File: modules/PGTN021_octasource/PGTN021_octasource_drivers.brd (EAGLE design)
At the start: 69.8 x 100.3 mm, 136 parts, among them IC1 TL084P, IC2 TL084P, IC3 TL084P, IC4 TL084P

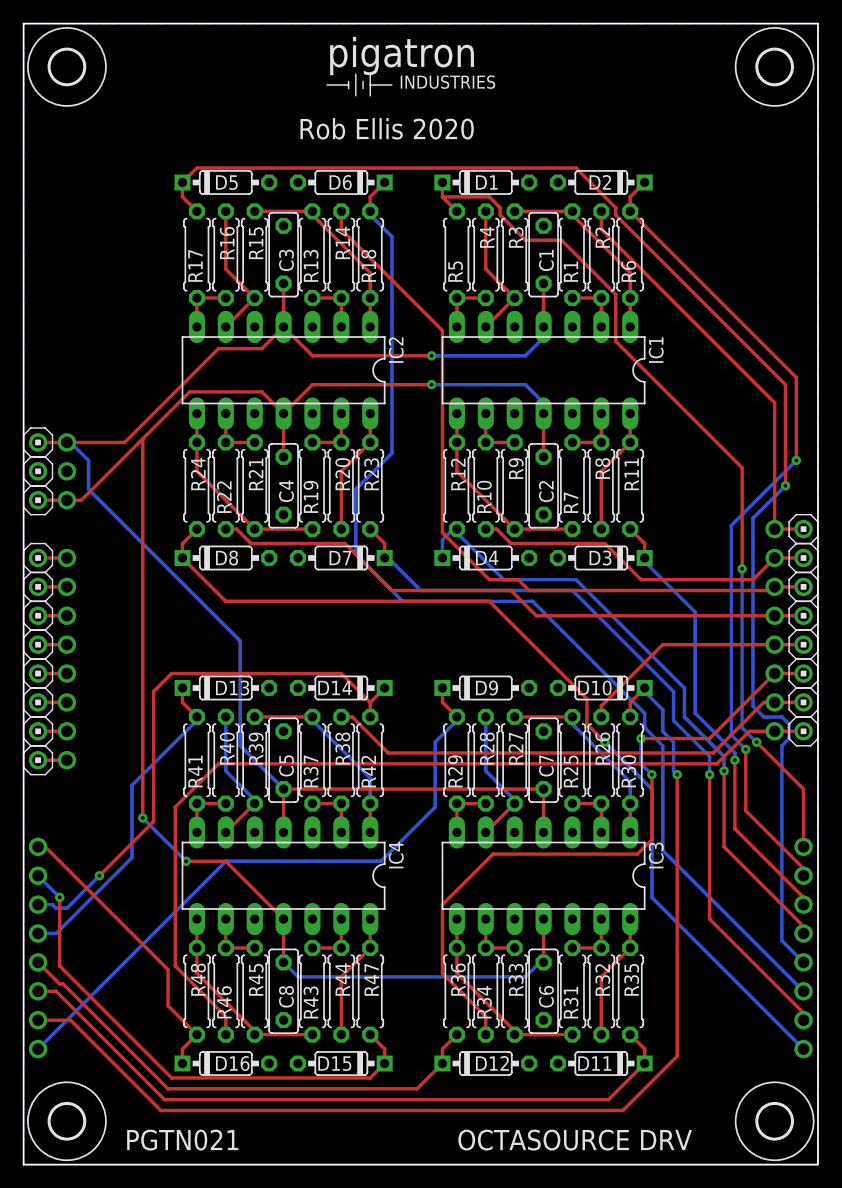
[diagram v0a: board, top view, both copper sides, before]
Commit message: Modified boards to fit together better
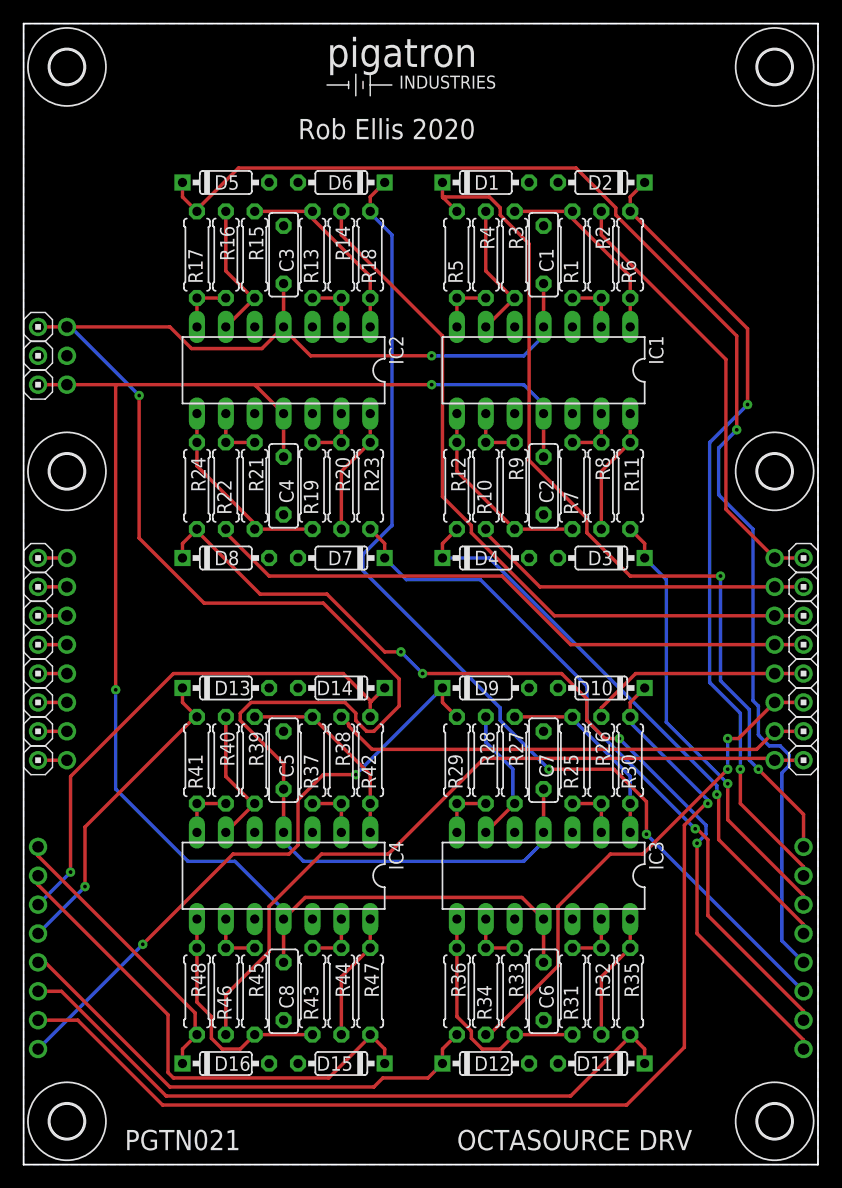
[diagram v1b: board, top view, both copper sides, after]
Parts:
- added U$4, U$5: (no value), mechanical:STANDOFF/3.0
- moved TRIG_IN 15.2 mm to (3.81, 53.3)
- moved TRIG_IN1 15.2 mm to (1.27, 53.3)
- moved GND 10.2 mm to (3.81, 71.1)
- moved GND1 10.2 mm to (1.27, 71.1)
- moved +12V 10.2 mm to (3.81, 73.7)
- moved +12V1 10.2 mm to (1.27, 73.7)
- moved -12V 10.2 mm to (3.81, 68.6)
- moved -12V1 10.2 mm to (1.27, 68.6)
- moved WAVE_POT 10.2 mm to (3.81, 50.8)
- moved WAVE_POT1 10.2 mm to (1.27, 50.8)
- moved RATE_POT 7.62 mm to (3.81, 45.7)
- moved RATE_POT1 7.62 mm to (1.27, 45.7)
- moved LENGTH_CV 7.62 mm to (3.81, 38.1)
- moved LENGTH_CV1 7.62 mm to (1.27, 38.1)
- moved LENGTH_POT 7.62 mm to (3.81, 40.6)
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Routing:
- net +12V: track 128.0 -> 166.5 mm, vias 1 -> 2
- net N$42: track 59.7 -> 44.7 mm
- net N$57: track 79.9 -> 65.3 mm
- net -12V: track 140.4 -> 144.7 mm, vias 3 -> 2
- net N$26: track 67.0 -> 62.9 mm
- net N$21: track 96.8 -> 92.9 mm, vias 0 -> 2
- net N$15: track 55.3 -> 51.7 mm
- net N$54: track 17.5 -> 20.8 mm
- net N$39: track 17.5 -> 20.8 mm
- net N$6: track 77.6 -> 80.4 mm
- net N$4: track 36.8 -> 39.3 mm
- net N$50: track 48.7 -> 46.7 mm
- net N$7: track 72.5 -> 70.6 mm
- net N$20: track 120.2 -> 118.6 mm
- net N$34: track 55.5 -> 54.1 mm, vias 0 -> 2
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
